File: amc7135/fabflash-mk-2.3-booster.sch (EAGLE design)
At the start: 22 parts, among them Q1 MOSFET-PCHANNELIRLML2244, U1 LM2735YMF

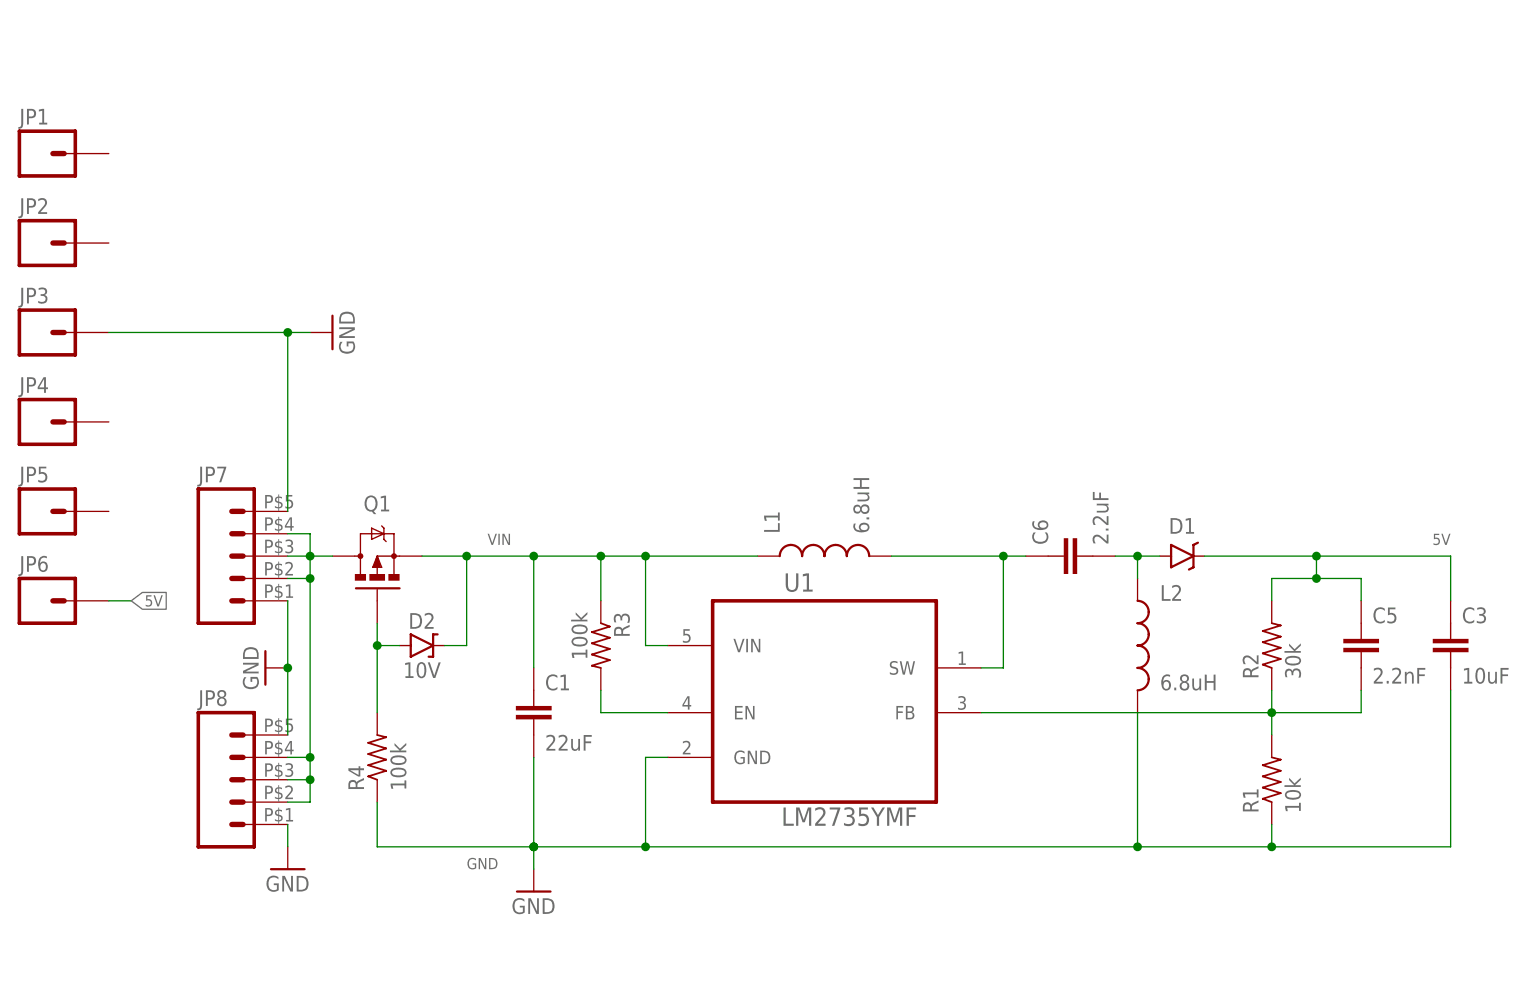
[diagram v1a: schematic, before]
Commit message: added #2 screw holes to each board and verified pins aligned correctly (had to flipflop 5v/gnd a few times)
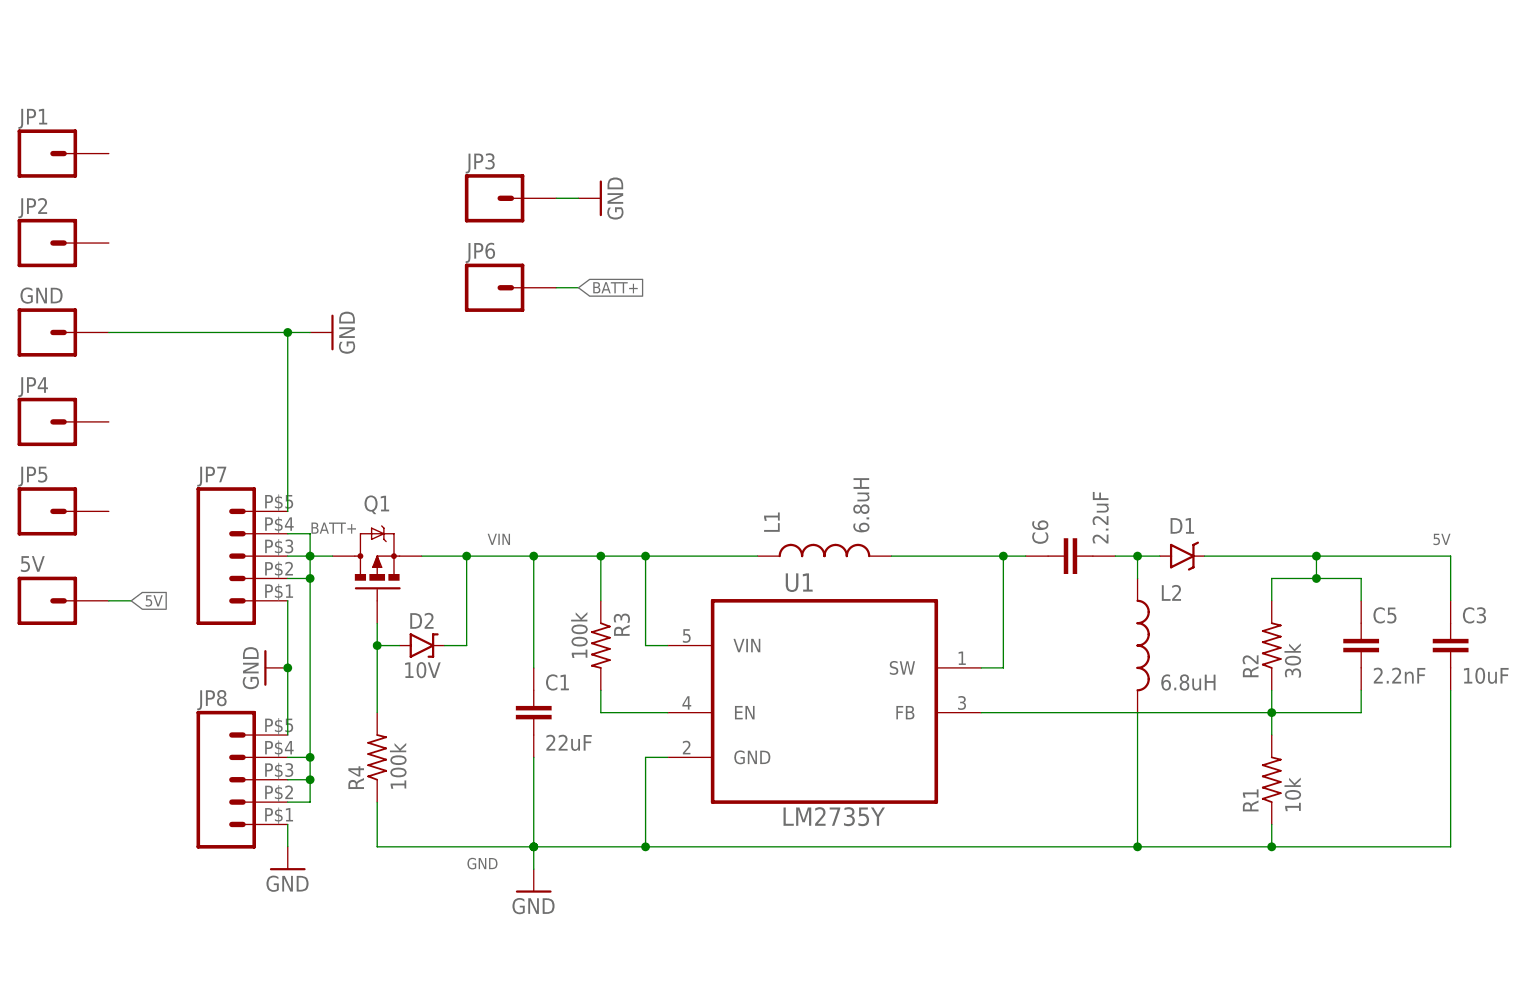
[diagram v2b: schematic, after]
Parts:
- added 5V, GND: M01PTH-0.9MM, A_butts:M01PTH-0.9MM
- D1: device A_butts:DIODE-SCHOTTKYSOD123 -> A_butts:DIODE-SCHOTTKYB340A
- JP3, JP6: value M01PTH-0.9MM-NS -> M01NOT-A-VIA-NOPE; device A_butts:M01PTH-0.9MM-NS -> A_butts:M01NOT-A-VIA-NOPE
- U1: value LM2735YMF -> LM2735Y
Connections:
- net 5V: now also 5V.1; no longer JP6.1
- net BATT+: now also JP6.1
- net GND: now also GND.1
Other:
- moved on the sheet: JP3, JP6
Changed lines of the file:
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@@
 <grid distance="100" unitdist="mil" unit="mil" style="lines" multiple="1" display="yes" altdistance="1" altunitdist="mm" altunit="mm"/>
 <layers>
-<layer number="1" name="Top" color="4" fill="1" visible="yes" active="no"/>
-<layer number="16" name="Bottom" color="1" fill="1" visible="yes" active="no"/>
-<layer number="17" name="Pads" color="2" fill="1" visible="yes" active="no"/>
-<layer number="18" name="Vias" color="2" fill="1" visible="yes" active="no"/>
-<layer number="19" name="Unrouted" color="6" fill="1" visible="yes" active="no"/>
-<layer number="20" name="Dimension" color="15" fill="1" visible="yes" active="no"/>
-<layer number="21" name="tPlace" color="7" fill="1" visible="yes" active="no"/>
-<layer number="22" name="bPlace" color="7" fill="1" visible="yes" active="no"/>
-<layer number="23" name="tOrigins" color="15" fill="1" visible="yes" active="no"/>
-<layer number="24" name="bOrigins" color="15" fill="1" visible="yes" active="no"/>
-<layer number="25" name="tNames" color="7" fill="1" visible="yes" active="no"/>
-<layer number="26" name="bNames" color="7" fill="1" visible="yes" active="no"/>
-<layer number="27" name="tValues" color="7" fill="1" visible="yes" active="no"/>
-<layer number="28" name="bValues" color="7" fill="1" visible="yes" active="no"/>
+<layer number="1" name="Top" color="4" fill="1" visible="no" active="no"/>
+<layer number="16" name="Bottom" color="1" fill="1" visible="no" active="no"/>
+<layer number="17" name="Pads" color="2" fill="1" visible="no" active="no"/>
+<layer number="18" name="Vias" color="2" fill="1" visible="no" active="no"/>
+<layer number="19" name="Unrouted" color="6" fill="1" visible="no" active="no"/>
+<layer number="20" name="Dimension" color="15" fill="1" visible="no" active="no"/>
+<layer number="21" name="tPlace" color="7" fill="1" visible="no" active="no"/>
+<layer number="22" name="bPlace" color="7" fill="1" visible="no" active="no"/>
+<layer number="23" name="tOrigins" color="15" fill="1" visible="no" active="no"/>
+<layer number="24" name="bOrigins" color="15" fill="1" visible="no" active="no"/>
+<layer number="25" name="tNames" color="7" fill="1" visible="no" active="no"/>
+<layer number="26" name="bNames" color="7" fill="1" visible="no" active="no"/>
+<layer number="27" name="tValues" color="7" fill="1" visible="no" active="no"/>
+<layer number="28" name="bValues" color="7" fill="1" visible="no" active="no"/>
 <layer number="29" name="tStop" color="7" fill="3" visible="no" active="no"/>
 <layer number="30" name="bStop" color="7" fill="6" visible="no" active="no"/>
@@
 <layer number="35" name="tGlue" color="7" fill="4" visible="no" active="no"/>
 <layer number="36" name="bGlue" color="7" fill="5" visible="no" active="no"/>
-<layer number="37" name="tTest" color="7" fill="1" visible="yes" active="no"/>
-<layer number="38" name="bTest" color="7" fill="1" visible="yes" active="no"/>
+<layer number="37" name="tTest" color="7" fill="1" visible="no" active="no"/>
+<layer number="38" name="bTest" color="7" fill="1" visible="no" active="no"/>
 <layer number="39" name="tKeepout" color="4" fill="11" visible="no" active="no"/>
 <layer number="40" name="bKeepout" color="1" fill="11" visible="no" active="no"/>
@@
 <layer number="44" name="Drills" color="7" fill="1" visible="no" active="no"/>
 <layer number="45" name="Holes" color="7" fill="1" visible="no" active="no"/>
-<layer number="46" name="Milling" color="3" fill="1" visible="yes" active="no"/>
-<layer number="47" name="Measures" color="7" fill="1" visible="yes" active="no"/>
-<layer number="48" name="Document" color="7" fill="1" visible="yes" active="no"/>
-<layer number="49" name="Reference" color="7" fill="1" visible="yes" active="no"/>
-<layer number="50" name="dxf" color="7" fill="1" visible="yes" active="no"/>
-<layer number="51" name="tDocu" color="7" fill="1" visible="yes" active="no"/>
-<layer number="52" name="bDocu" color="7" fill="1" visible="yes" active="no"/>
-<layer number="53" name="tGND_GNDA" color="7" fill="9" visible="yes" active="no"/>
-<layer number="54" name="bGND_GNDA" color="1" fill="9" visible="yes" active="no"/>
-<layer number="56" name="wert" color="7" fill="1" visible="yes" active="no"/>
-<layer number="57" name="tCAD" color="7" fill="1" visible="yes" active="no"/>
+<layer number="46" name="Milling" color="3" fill="1" visible="no" active="no"/>
+<layer number="47" name="Measures" color="7" fill="1" visible="no" active="no"/>
+<layer number="48" name="Document" color="7" fill="1" visible="no" active="no"/>
+<layer number="49" name="Reference" color="7" fill="1" visible="no" active="no"/>
+<layer number="50" name="dxf" color="7" fill="1" visible="no" active="no"/>
+<layer number="51" name="tDocu" color="7" fill="1" visible="no" active="no"/>
+<layer number="52" name="bDocu" color="7" fill="1" visible="no" active="no"/>
+<layer number="53" name="tGND_GNDA" color="7" fill="9" visible="no" active="no"/>
+<layer number="54" name="bGND_GNDA" color="1" fill="9" visible="no" active="no"/>
+<layer number="56" name="wert" color="7" fill="1" visible="no" active="no"/>
+<layer number="57" name="tCAD" color="7" fill="1" visible="no" active="no"/>
 <layer number="91" name="Nets" color="2" fill="1" visible="yes" active="yes"/>
 <layer number="92" name="Busses" color="1" fill="1" visible="yes" active="yes"/>
@@
 </classes>
 <parts>
-<part name="U1" library="A_butts" deviceset="LM2735YMF" device=""/>
+<part name="U1" library="A_butts" deviceset="LM2735YMF" device="" value="LM2735Y"/>
 <part name="GND1" library="A_butts" deviceset="GND" device=""/>
 <part name="C1" library="A_butts" deviceset="CAPACITOR-CERAMIC" device="C0805" value="22uF"/>
@@
 <part name="C6" library="A_butts" deviceset="CAPACITOR-CERAMIC" device="C0805" value="2.2uF"/>
 <part name="R2" library="A_butts" deviceset="RESISTOR" device="R0603" value="30k"/>
-<part name="D1" library="A_butts" deviceset="DIODE-SCHOTTKY" device="SOD123" value="B340A"/>
+<part name="D1" library="A_butts" deviceset="DIODE-SCHOTTKY" device="B340A" value="B340A"/>
 <part name="L1" library="A_butts" deviceset="INDUCTOR" device="TAIYO-YUDEN-40XX" value="6.8uH"/>
 <part name="L2" library="A_butts" deviceset="INDUCTOR" device="TAIYO-YUDEN-40XX" value="6.8uH"/>
@@
 <part name="JP1" library="A_butts" deviceset="M01" device="PTH-0.9MM-NS"/>
 <part name="JP2" library="A_butts" deviceset="M01" device="PTH-0.9MM-NS"/>
-<part name="JP3" library="A_butts" deviceset="M01" device="PTH-0.9MM-NS"/>
+<part name="GND" library="A_butts" deviceset="M01" device="PTH-0.9MM" value="M01PTH-0.9MM"/>
 <part name="JP4" library="A_butts" deviceset="M01" device="PTH-0.9MM-NS"/>
 <part name="JP5" library="A_butts" deviceset="M01" device="PTH-0.9MM-NS"/>
-<part name="JP6" library="A_butts" deviceset="M01" device="PTH-0.9MM-NS"/>
+<part name="5V" library="A_butts" deviceset="M01" device="PTH-0.9MM" value="M01PTH-0.9MM"/>
 <part name="JP7" library="A_butts" deviceset="M05" device="SMD-SHORT-2MM"/>
 <part name="GND3" library="A_butts" deviceset="GND" device=""/>
 <part name="JP8" library="A_butts" deviceset="M05" device="SMD-SHORT-2MM"/>
 <part name="GND5" library="A_butts" deviceset="GND" device=""/>
+<part name="JP3" library="A_butts" deviceset="M01" device="NOT-A-VIA-NOPE"/>
+<part name="JP6" library="A_butts" deviceset="M01" device="NOT-A-VIA-NOPE"/>
+<part name="GND4" library="A_butts" deviceset="GND" device=""/>
 </parts>
 <sheets>
@@
 <instance part="JP1" gate="G$1" x="-20.32" y="106.68"/>
 <instance part="JP2" gate="G$1" x="-20.32" y="96.52"/>
-<instance part="JP3" gate="G$1" x="-20.32" y="86.36"/>
+<instance part="GND" gate="G$1" x="-20.32" y="86.36"/>
 <instance part="JP4" gate="G$1" x="-20.32" y="76.2"/>
 <instance part="JP5" gate="G$1" x="-20.32" y="66.04"/>
-<instance part="JP6" gate="G$1" x="-20.32" y="55.88"/>
+<instance part="5V" gate="G$1" x="-20.32" y="55.88"/>
 <instance part="JP7" gate="G$1" x="0" y="60.96"/>
 <instance part="GND3" gate="1" x="5.08" y="48.26" rot="MR90"/>
 <instance part="JP8" gate="G$1" x="0" y="35.56"/>
 <instance part="GND5" gate="1" x="7.62" y="25.4"/>
+<instance part="JP3" gate="G$1" x="30.48" y="101.6"/>
+<instance part="JP6" gate="G$1" x="30.48" y="91.44"/>
+<instance part="GND4" gate="1" x="43.18" y="101.6" rot="R90"/>
 </instances>
 <busses>
@@
 <wire x1="-12.7" y1="86.36" x2="7.62" y2="86.36" width="0.1524" layer="91"/>
 <pinref part="GND2" gate="1" pin="GND"/>
-<pinref part="JP3" gate="G$1" pin="1"/>
+<pinref part="GND" gate="G$1" pin="1"/>
 <pinref part="JP7" gate="G$1" pin="5"/>
 <wire x1="7.62" y1="86.36" x2="10.16" y2="86.36" width="0.1524" layer="91"/>
@@
 <pinref part="GND5" gate="1" pin="GND"/>
 <wire x1="7.62" y1="30.48" x2="7.62" y2="27.94" width="0.1524" layer="91"/>
+</segment>
+<segment>
+<pinref part="JP3" gate="G$1" pin="1"/>
+<pinref part="GND4" gate="1" pin="GND"/>
+<wire x1="38.1" y1="101.6" x2="40.64" y2="101.6" width="0.1524" layer="91"/>
 </segment>
 </net>
@@
 <wire x1="-12.7" y1="55.88" x2="-10.16" y2="55.88" width="0.1524" layer="91"/>
 <label x="-10.16" y="55.88" size="1.27" layer="95" xref="yes"/>
-<pinref part="JP6" gate="G$1" pin="1"/>
+<pinref part="5V" gate="G$1" pin="1"/>
 </segment>
 <segment>
@@
 <wire x1="7.62" y1="35.56" x2="10.16" y2="35.56" width="0.1524" layer="91"/>
 <junction x="10.16" y="35.56"/>
-</segment>
-</net>
+<label x="10.16" y="63.5" size="1.27" layer="95"/>
+</segment>
+<segment>
+<pinref part="JP6" gate="G$1" pin="1"/>
+<wire x1="38.1" y1="91.44" x2="40.64" y2="91.44" width="0.1524" layer="91"/>
+<label x="40.64" y="91.44" size="1.27" layer="95" xref="yes"/>
+</segment>
+</net>

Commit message: booster using 4x0.1in headers instead of 5x2mm, along with routing to smooth edges
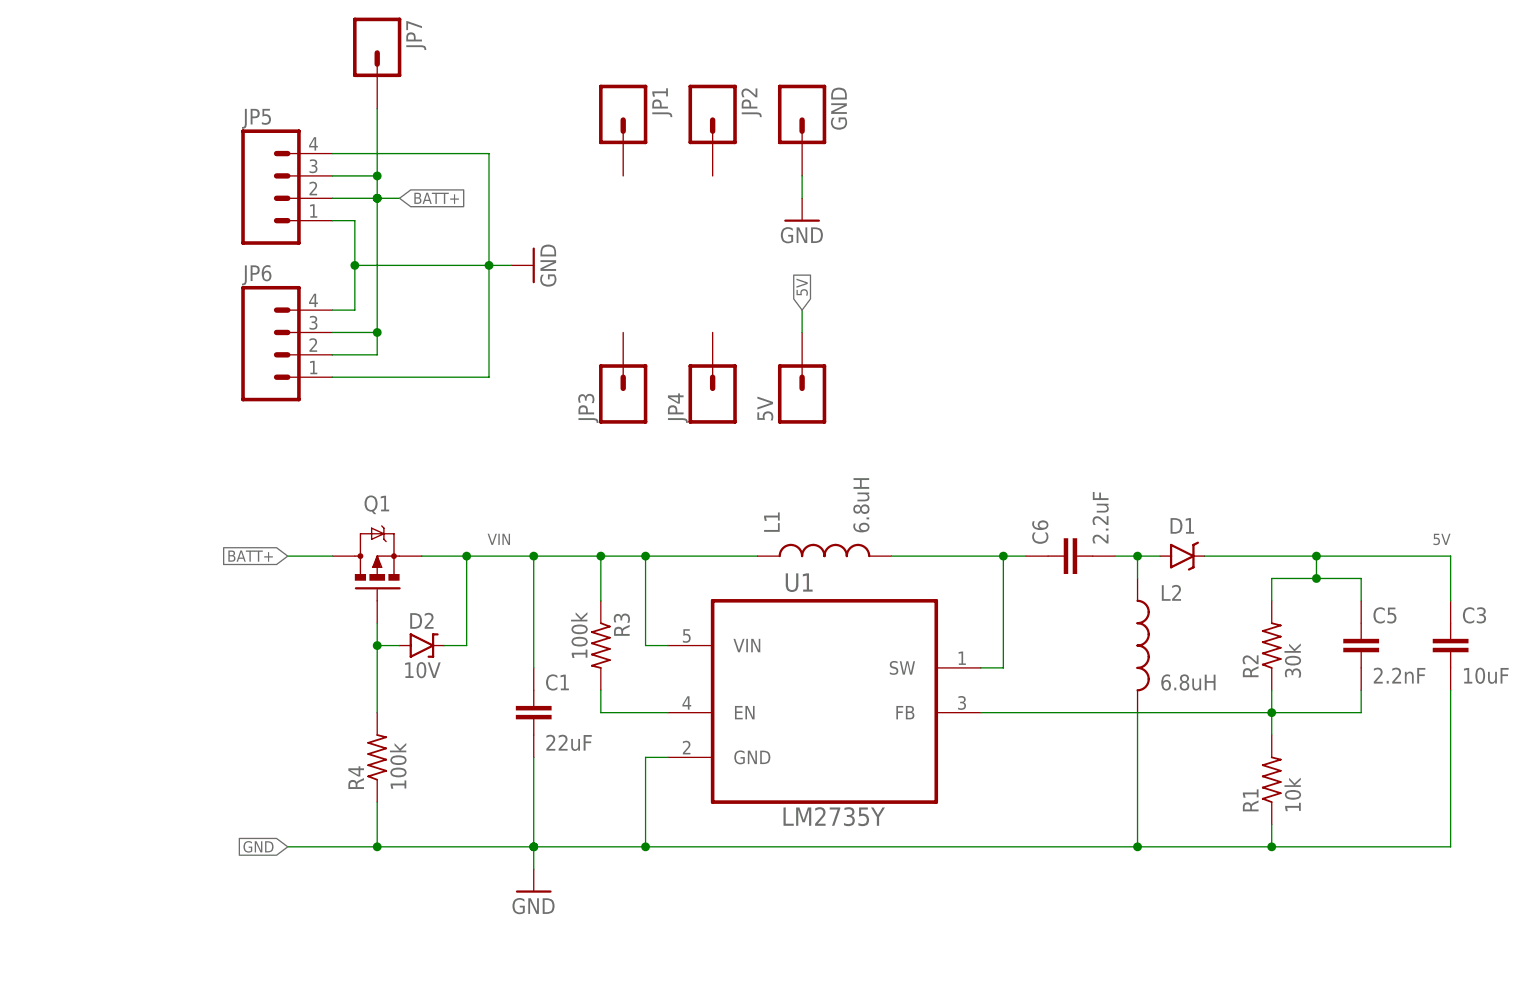
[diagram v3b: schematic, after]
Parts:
- removed JP8: (no value), A_butts:M05SMD-SHORT-2MM
- JP3: value M01NOT-A-VIA-NOPE -> M01PTH-0.9MM-NS; device A_butts:M01NOT-A-VIA-NOPE -> A_butts:M01PTH-0.9MM-NS
- JP5: value M01PTH-0.9MM-NS -> M04SMD-SHORT-NS; device A_butts:M01PTH-0.9MM-NS -> A_butts:M04SMD-SHORT-NS
- JP6: value M01NOT-A-VIA-NOPE -> M04SMD-SHORT-NS; device A_butts:M01NOT-A-VIA-NOPE -> A_butts:M04SMD-SHORT-NS
- JP7: value (none) -> M01NOT-A-VIA-NOPE; device A_butts:M05SMD-SHORT-2MM -> A_butts:M01NOT-A-VIA-NOPE
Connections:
- net BATT+: now also JP5.2, JP5.3, JP6.2, JP6.3, JP7.1; no longer JP6.1, JP7.2, JP7.3, JP7.4, JP8.2, JP8.3, JP8.4
- net GND: now also JP5.1, JP5.4, JP6.1, JP6.4; no longer JP3.1, JP7.1, JP7.5, JP8.1, JP8.5
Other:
- moved on the sheet: 5V, GND, JP1, JP2, JP3, JP4

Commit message: finishing touches hopefully
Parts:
- D1: device A_butts:DIODE-SCHOTTKYB340A -> A_butts:DIODE-SCHOTTKYSMA
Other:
- moved on the sheet: C5, R1, R2, U1
